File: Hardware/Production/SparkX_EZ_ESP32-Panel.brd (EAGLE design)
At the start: 187.2 x 95.5 mm, 1506 parts, among them Q1 MBT3904DW1T1, Q10 MBT3904DW1T1, Q11 MBT3904DW1T1, Q12 MBT3904DW1T1, Q13 MBT3904DW1T1, Q14 MBT3904DW1T1, Q15 MBT3904DW1T1, Q16 MBT3904DW1T1, Q17 MBT3904DW1T1, Q18 MBT3904DW1T1, Q19 MBT3904DW1T1, Q2 MBT3904DW1T1, Q20 MBT3904DW1T1, Q3 MBT3904DW1T1, Q4 MBT3904DW1T1, Q5 MBT3904DW1T1, Q6 MBT3904DW1T1, Q7 MBT3904DW1T1, Q8 MBT3904DW1T1, Q9 MBT3904DW1T1, U1 MIC5219 3.3V, U10 W25QXX128MBIT-6X5-SKINNY_CENT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, U11 CP2102N, U12 MIC5219 3.3V, U13 ESP32, U14 W25QXX128MBIT-6X5-SKINNY_CENT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, U15 CP2102N, U16 MIC5219 3.3V, U17 ESP32, U18 W25QXX128MBIT-6X5-SKINNY_CENT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, U19 CP2102N, U2 ESP32, U20 MIC5219 3.3V, U21 ESP32, U22 W25QXX128MBIT-6X5-SKINNY_CENT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, U23 CP2102N, U24 MIC5219 3.3V, U25 ESP32, U26 W25QXX128MBIT-6X5-SKINNY_CENT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, U27 CP2102N, U28 MIC5219 3.3V, U29 ESP32, U3 W25QXX128MBIT-6X5-SKINNY_CENT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, U30 W25QXX128MBIT-6X5-SKINNY_CENT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, U31 CP2102N, U32 MIC5219 3.3V, U33 ESP32, U34 W25QXX128MBIT-6X5-SKINNY_CENT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, U35 CP2102N, U36 MIC5219 3.3V, U37 ESP32, U38 W25QXX128MBIT-6X5-SKINNY_CENT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, U39 CP2102N, U4 CP2102N, U40 MIC5219 3.3V, U41 ESP32, U42 W25QXX128MBIT-6X5-SKINNY_CENT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, U43 CP2102N, U44 MIC5219 3.3V, U45 ESP32, U46 W25QXX128MBIT-6X5-SKINNY_CENT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, U47 CP2102N, U48 MIC5219 3.3V, U49 ESP32, U5 ESP32, U50 W25QXX128MBIT-6X5-SKINNY_CENT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, U51 CP2102N, U52 MIC5219 3.3V, U53 ESP32, U54 W25QXX128MBIT-6X5-SKINNY_CENT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, U55 CP2102N, U56 MIC5219 3.3V, U57 ESP32, U58 W25QXX128MBIT-6X5-SKINNY_CENT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, U59 CP2102N, U6 W25QXX128MBIT-6X5-SKINNY_CENT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, U60 MIC5219 3.3V, U61 ESP32, U62 W25QXX128MBIT-6X5-SKINNY_CENT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, U63 CP2102N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

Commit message: Post-review updates
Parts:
- C1, C122, C147, C172, C197, C222, C247, C272, C297, C322, C347, C372, C397, C422, C447, C47, C472, C497, C72, C97: value 0.1uF -> 2.2uF
- moved C204 1.17 mm to (139.6, 20.5)
- moved C229 1.17 mm to (155.9, 20.5)
- moved C179 1.17 mm to (123.4, 20.5)
- moved C329 1.17 mm to (49.8, 61.3)
- moved C354 1.17 mm to (66.1, 61.3)
- moved C379 1.17 mm to (82.4, 61.3)
- moved C404 1.17 mm to (98.6, 61.3)
- moved C429 1.17 mm to (114.9, 61.3)
- moved C279 1.17 mm to (17.3, 61.3)
- moved C29 1.17 mm to (25.8, 20.5)
- moved C254 1.17 mm to (1.08, 61.3)
- moved C11 1.17 mm to (9.59, 20.5)
- moved C304 1.17 mm to (33.6, 61.3)
- moved C54 1.17 mm to (42.1, 20.5)
- moved C79 1.17 mm to (58.4, 20.5)
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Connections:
- net CS1: now also U2.17; no longer U2.15
- net CS10: now also U13.17; no longer U13.15
- net CS11: now also U13.20; no longer U13.16
- net CS13: now also U17.17; no longer U17.15
- net CS14: now also U17.20; no longer U17.16
- net CS16: now also U21.17; no longer U21.15
- net CS17: now also U21.20; no longer U21.16
- net CS19: now also U25.17; no longer U25.15
- net CS2: now also U2.20; no longer U2.16
- net CS20: now also U25.20; no longer U25.16
- net CS22: now also U29.17; no longer U29.15
- net CS23: now also U29.20; no longer U29.16
- net CS25: now also U33.17; no longer U33.15
- net CS26: now also U33.20; no longer U33.16
- net CS28: now also U37.17; no longer U37.15
- net CS29: now also U37.20; no longer U37.16
- net CS31: now also U41.17; no longer U41.15
- net CS32: now also U41.20; no longer U41.16
- net CS34: now also U45.17; no longer U45.15
- net CS35: now also U45.20; no longer U45.16
- net CS37: now also U49.17; no longer U49.15
- net CS38: now also U49.20; no longer U49.16
- net CS4: now also U5.17; no longer U5.15
- net CS40: now also U53.17; no longer U53.15
- net CS41: now also U53.20; no longer U53.16
- net CS43: now also U57.17; no longer U57.15
- net CS44: now also U57.20; no longer U57.16
- net CS46: now also U61.17; no longer U61.15
- net CS47: now also U61.20; no longer U61.16
- net CS49: now also U65.17; no longer U65.15
- net CS5: now also U5.20; no longer U5.16
- net CS50: now also U65.20; no longer U65.16
- net CS52: now also U69.17; no longer U69.15
- net CS53: now also U69.20; no longer U69.16
- net CS55: now also U73.17; no longer U73.15
- net CS56: now also U73.20; no longer U73.16
- net CS58: now also U77.17; no longer U77.15
- net CS59: now also U77.20; no longer U77.16
- net CS7: now also U9.17; no longer U9.15
- net CS8: now also U9.20; no longer U9.16
- net GPIO0: now also U2.16; no longer U2.10
- net GPIO1: now also U2.15; no longer U2.11
- net GPIO10: now also U21.16; no longer U21.10
- net GPIO11: now also U21.15; no longer U21.11
- net GPIO12: now also U25.16; no longer U25.10
- net GPIO13: now also U25.15; no longer U25.11
- net GPIO14: now also U29.16; no longer U29.10
- net GPIO15: now also U29.15; no longer U29.11
- net GPIO16: now also U33.16; no longer U33.10
- net GPIO17: now also U33.15; no longer U33.11
- net GPIO18: now also U37.16; no longer U37.10
- net GPIO19: now also U37.15; no longer U37.11
- net GPIO2: now also U5.16; no longer U5.10
- net GPIO20: now also U41.16; no longer U41.10
- net GPIO21: now also U41.15; no longer U41.11
- net GPIO22: now also U45.16; no longer U45.10
- net GPIO23: now also U45.15; no longer U45.11
- net GPIO24: now also U49.16; no longer U49.10
- net GPIO25: now also U49.15; no longer U49.11
- net GPIO26: now also U53.16; no longer U53.10
- net GPIO27: now also U53.15; no longer U53.11
- net GPIO28: now also U57.16; no longer U57.10
- net GPIO29: now also U57.15; no longer U57.11
- net GPIO3: now also U5.15; no longer U5.11
- net GPIO30: now also U61.16; no longer U61.10
- net GPIO31: now also U61.15; no longer U61.11
- net GPIO32: now also U65.16; no longer U65.10
- net GPIO33: now also U65.15; no longer U65.11
- net GPIO34: now also U69.16; no longer U69.10
- net GPIO35: now also U69.15; no longer U69.11
- net GPIO36: now also U73.16; no longer U73.10
- net GPIO37: now also U73.15; no longer U73.11
- net GPIO38: now also U77.16; no longer U77.10
- net GPIO39: now also U77.15; no longer U77.11
- net GPIO4: now also U9.16; no longer U9.10
- net GPIO5: now also U9.15; no longer U9.11
- net GPIO6: now also U13.16; no longer U13.10
- net GPIO7: now also U13.15; no longer U13.11
- net GPIO8: now also U17.16; no longer U17.10
- net GPIO9: now also U17.15; no longer U17.11
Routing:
- net SDA9: track 69.7 -> 50.0 mm
- net SDA8: track 69.7 -> 50.0 mm
- net SDA4: track 69.7 -> 50.0 mm
- net SDA13: track 69.7 -> 50.0 mm
- net SDA12: track 69.7 -> 50.0 mm
- net SDA1: track 69.7 -> 50.0 mm
- net SDA: track 69.7 -> 50.0 mm
- net SDA11: track 69.7 -> 50.0 mm
- net SDA10: track 69.7 -> 50.0 mm
- net SDA3: track 69.7 -> 50.0 mm
- net SDA2: track 69.7 -> 50.0 mm
- net SDA17: track 69.7 -> 50.0 mm
- net SDA16: track 69.7 -> 50.0 mm
- net SDA15: track 69.7 -> 50.0 mm
- net SDA14: track 69.7 -> 50.0 mm
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
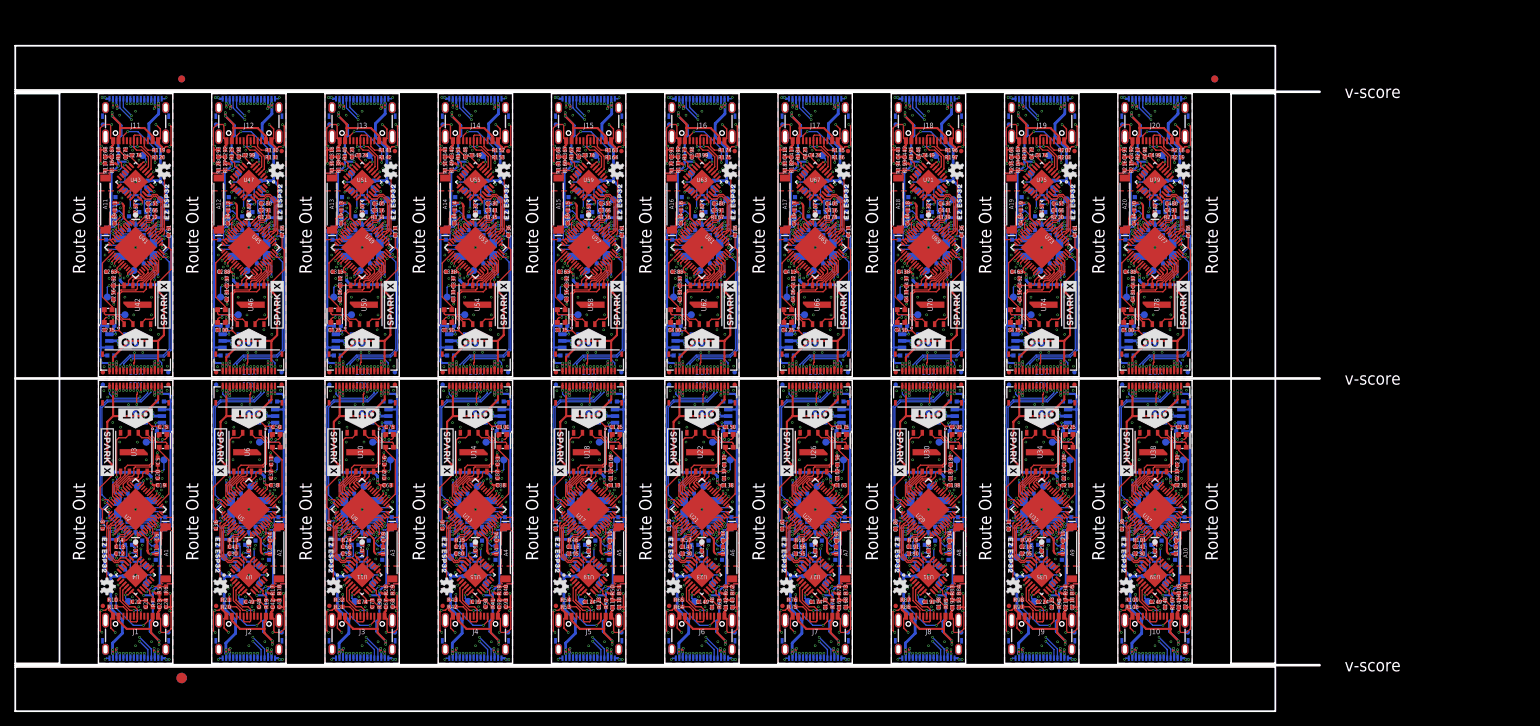
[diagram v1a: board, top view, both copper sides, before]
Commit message: Gapless production panel
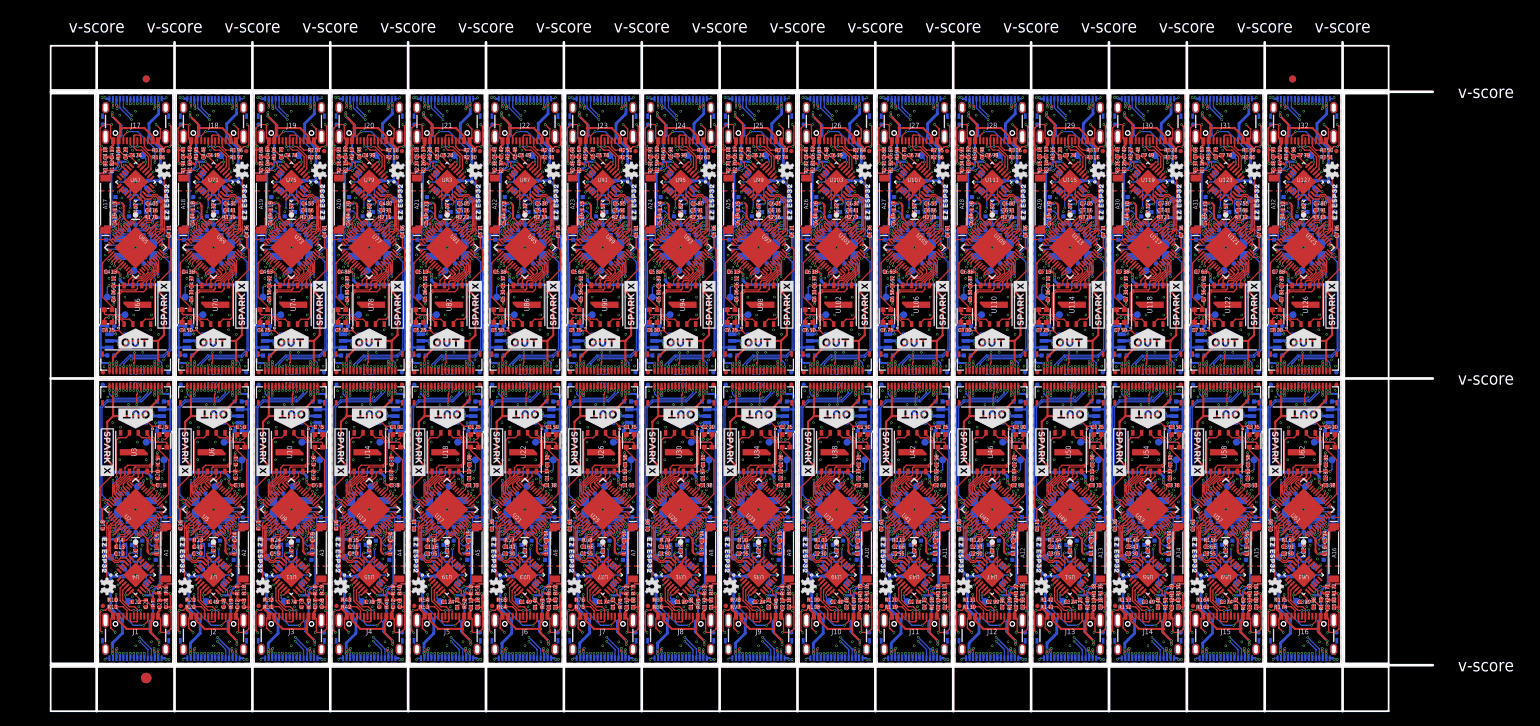
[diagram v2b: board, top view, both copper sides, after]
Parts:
- added !BOOT!20, !BOOT!21, !BOOT!22, !BOOT!23, !BOOT!24, !BOOT!25, !BOOT!26, !BOOT!27, !BOOT!28, !BOOT!29, !BOOT!30, !BOOT!31, !RESET!20, !RESET!21, !RESET!22, !RESET!23, !RESET!24, !RESET!25, !RESET!26, !RESET!27, !RESET!28, !RESET!29, !RESET!30, !RESET!31, FLASH_VDD20, FLASH_VDD21, FLASH_VDD22, FLASH_VDD23, FLASH_VDD24, FLASH_VDD25, FLASH_VDD26, FLASH_VDD27, FLASH_VDD28, FLASH_VDD29, FLASH_VDD30, FLASH_VDD31, LED_DO20, LED_DO21, LED_DO22, LED_DO23, LED_DO24, LED_DO25, LED_DO26, LED_DO27, LED_DO28, LED_DO29, LED_DO30, LED_DO31, RXT20, RXT21, RXT22, RXT23, RXT24, RXT25, RXT26, RXT27, RXT28, RXT29, RXT30, RXT31, TXT20, TXT21, TXT22, TXT23, TXT24, TXT25, TXT26, TXT27, TXT28, TXT29, TXT30, TXT31, USB_3V21, USB_3V22, USB_3V23, USB_3V24, USB_3V25, USB_3V26, USB_3V27, USB_3V28, USB_3V29, USB_3V30, USB_3V31, USB_3V32: TEST-POINT3X4, SparkFun-Connectors:PAD.03X.04
- added A21, A22, A23, A24, A25, A26, A27, A28, A29, A30, A31, A32: ANTENNA2.4GHZ-8.0X1.0MM, SparkFun-RF:ANT-2.4GHZ-8.0X1.0MM
- added C501, C502, C526, C527, C551, C552, C576, C577, C601, C602, C626, C627, C651, C652, C676, C677, C701, C702, C726, C727, C751, C752, C776, C777: 12pF, SparkFun-Capacitors:0402-TIGHT
- added C503, C504, C528, C529, C553, C554, C578, C579, C603, C604, C628, C629, C653, C654, C678, C679, C703, C704, C728, C729, C753, C754, C778, C779: 270pF, SparkFun-Capacitors:0402-TIGHT
- added C505, C530, C555, C580, C605, C630, C655, C680, C705, C730, C755, C780: 10nF, SparkFun-Capacitors:0402-TIGHT
- added C506, C508, C509, C511, C513, C517, C524, C525, C531, C533, C534, C536, C538, C542, C549, C550, C556, C558, C559, C561, C563, C567, C574, C575, C581, C583, C584, C586, C588, C592, C599, C600, C606, C608, C609, C611, C613, C617, C624, C625, C631, C633, C634, C636, C638, C642, C649, C650, C656, C658, C659, C661, C663, C667, C674, C675, C681, C683, C684, C686, C688, C692, C699, C700, C706, C708, C709, C711, C713, C717, C724, C725, C731, C733, C734, C736, C738, C742, C749, C750, C756, C758, C759, C761, C763, C767, C774, C775, C781, C783, C784, C786, C788, C792, C799, C800: 0.1uF, SparkFun-Capacitors:0402-TIGHT
- added C507, C532, C557, C582, C607, C632, C657, C682, C707, C732, C757, C782: 100pF, SparkFun-Capacitors:0402-TIGHT
- added C510, C535, C560, C585, C610, C635, C660, C685, C710, C735, C760, C785: 10uF, SparkFun-Capacitors:0402-TIGHT
- added C512, C537, C562, C587, C612, C637, C662, C687, C712, C737, C762, C787: 1.0uF, SparkFun-Capacitors:0402-TIGHT
- added C514, C515, C539, C540, C564, C565, C589, C590, C614, C615, C639, C640, C664, C665, C689, C690, C714, C715, C739, C740, C764, C765, C789, C790: 15pF, SparkFun-Capacitors:0402-TIGHT
- added C516, C541, C566, C591, C616, C641, C666, C691, C716, C741, C766, C791: 3.0nF, SparkFun-Capacitors:0402-TIGHT
- added C518, C523, C543, C548, C568, C573, C593, C598, C618, C623, C643, C648, C668, C673, C693, C698, C718, C723, C743, C748, C768, C773, C793, C798: 4.7uF, SparkFun-Capacitors:0402-TIGHT
- added C519, C520, C544, C545, C569, C570, C594, C595, C619, C620, C644, C645, C669, C670, C694, C695, C719, C720, C744, C745, C769, C770, C794, C795: DNP, SparkFun-Capacitors:0402-TIGHT
- added C521, C522, C546, C547, C571, C572, C596, C597, C621, C622, C646, C647, C671, C672, C696, C697, C721, C722, C746, C747, C771, C772, C796, C797: 2.2uF, SparkFun-Capacitors:0402-TIGHT
- added D21, D22, D23, D24, D25, D26, D27, D28, D29, D30, D31, D32: WS2812_2020, SparkFun-LED:WS2812-2020
- added FD100, FD101, FD102, FD103, FD104, FD105, FD106, FD107, FD108, FD109, FD110, FD111, FD112, FD113, FD114, FD115, FD116, FD117, FD118, FD119, FD120, FD121, FD122, FD123, FD124, FD125, FD126, FD127, FD128, FD81, FD82, FD83, FD84, FD85, FD86, FD87, FD88, FD89, FD90, FD91, FD92, FD93, FD94, FD95, FD96, FD97, FD98, FD99: FIDUCIALUFIDUCIAL, SparkFun-Aesthetics:FIDUCIAL-MICRO
- added IN20, IN21, IN22, IN23, IN24, IN25, IN26, IN27, IN28, IN29, IN30, IN31, OUT20, OUT21, OUT22, OUT23, OUT24, OUT25, OUT26, OUT27, OUT28, OUT29, OUT30, OUT31: FPC_16_0.5MM_BACKFLIP, New_Parts_Connectors:FPC_16_DOUBLESIDED_BACKFLIP
- added J21, J22, J23, J24, J25, J26, J27, J28, J29, J30, J31, J32: (no value), SparkFun-Connectors:USB-C-16P_4LAYER-PADS
- added L21, L22, L23, L24, L25, L26, L27, L28, L29, L30, L31, L32: 0, SparkFun-Resistors:0402-TIGHT
- added LOGO41, LOGO42, LOGO43, LOGO44, LOGO45, LOGO46, LOGO47, LOGO48, LOGO49, LOGO50, LOGO51, LOGO52, LOGO53, LOGO54, LOGO55, LOGO56, LOGO57, LOGO58, LOGO59, LOGO60, LOGO61, LOGO62, LOGO63, LOGO64: OSHW-LOGOMINI, SparkFun-Aesthetics:OSHW-LOGO-MINI
- added Q21, Q22, Q23, Q24, Q25, Q26, Q27, Q28, Q29, Q30, Q31, Q32: MBT3904DW1T1, SparkFun-DiscreteSemi:SC70-6
- added R221, R223, R224, R225, R232, R234, R235, R236, R243, R245, R246, R247, R254, R256, R257, R258, R265, R267, R268, R269, R276, R278, R279, R280, R287, R289, R290, R291, R298, R300, R301, R302, R309, R311, R312, R313, R320, R322, R323, R324, R331, R333, R334, R335, R342, R344, R345, R346: 10k, SparkFun-Resistors:0402-TIGHT
- added R222, R233, R244, R255, R266, R277, R288, R299, R310, R321, R332, R343: 20k, SparkFun-Resistors:0402-TIGHT
- added R226, R237, R248, R259, R270, R281, R292, R303, R314, R325, R336, R347: 22k, SparkFun-Resistors:0402-TIGHT
- added R227, R238, R249, R260, R271, R282, R293, R304, R315, R326, R337, R348: 33k, SparkFun-Resistors:0402-TIGHT
- added R228, R239, R250, R261, R272, R283, R294, R305, R316, R327, R338, R349: 2.2k, SparkFun-Resistors:0402-TIGHT
- added R229, R230, R240, R241, R251, R252, R262, R263, R273, R274, R284, R285, R295, R296, R306, R307, R317, R318, R328, R329, R339, R340, R350, R351: 5.1k, SparkFun-Resistors:0402-TIGHT
- added R231, R242, R253, R264, R275, R286, R297, R308, R319, R330, R341, R352: 100k, SparkFun-Resistors:0402-TIGHT
- added U$261, U$262, U$274, U$275, U$287, U$288, U$300, U$301, U$313, U$314, U$326, U$327, U$339, U$340, U$352, U$353, U$365, U$366, U$378, U$379, U$391, U$392, U$404, U$405: SPARKX-LOGO3, SparkX:SPARKX-SMALL
- added U$263, U$276, U$289, U$302, U$315, U$328, U$341, U$354, U$367, U$380, U$393, U$406: (no value), output:#IN#0
- added U$264, U$277, U$290, U$303, U$316, U$329, U$342, U$355, U$368, U$381, U$394, U$407: (no value), output:#OUT#0
- added U$265, U$266, U$278, U$279, U$291, U$292, U$304, U$305, U$317, U$318, U$330, U$331, U$343, U$344, U$356, U$357, U$369, U$370, U$382, U$383, U$395, U$396, U$408, U$409: (no value), output:EZ_ESP320
- added U$267, U$280, U$293, U$306, U$319, U$332, U$345, U$358, U$371, U$384, U$397, U$410: (no value), output:#TXT#0
- added U$268, U$281, U$294, U$307, U$320, U$333, U$346, U$359, U$372, U$385, U$398, U$411: (no value), output:#RXT#0
- added U$269, U$282, U$295, U$308, U$321, U$334, U$347, U$360, U$373, U$386, U$399, U$412: (no value), output:##BOOT##0
- added U$270, U$283, U$296, U$309, U$322, U$335, U$348, U$361, U$374, U$387, U$400, U$413: (no value), output:##RESET##0
- added U$271, U$284, U$297, U$310, U$323, U$336, U$349, U$362, U$375, U$388, U$401, U$414: (no value), output:#USB_3V3#0
- added U$272, U$285, U$298, U$311, U$324, U$337, U$350, U$363, U$376, U$389, U$402, U$415: (no value), output:#FVDD#0
- added U$273, U$286, U$299, U$312, U$325, U$338, U$351, U$364, U$377, U$390, U$403, U$416: (no value), output:#LED_DO#0
- added U100, U104, U108, U112, U116, U120, U124, U128, U84, U88, U92, U96: MIC5219 3.3V, SparkFun-IC-Power:SOT23-5
- added U101, U105, U109, U113, U117, U121, U125, U81, U85, U89, U93, U97: ESP32, SparkFun-RF:QFN48-0.4MM
- added U102, U106, U110, U114, U118, U122, U126, U82, U86, U90, U94, U98: W25QXX128MBIT-6X5-SKINNY_CENTER, SparkFun-IC-Memory:WSON-8-6X5-SKINNY_CENTERPAD
- added U103, U107, U111, U115, U119, U123, U127, U83, U87, U91, U95, U99: CP2102N, SparkFun-IC-Comms:QFN24
- added X41, X43, X45, X47, X49, X51, X53, X55, X57, X59, X61, X63: 40MHz, SparkFun-Clocks:CRYSTAL-SMD-2X2.5MM
- added X42, X44, X46, X48, X50, X52, X54, X56, X58, X60, X62, X64: 32.768kHz, SparkFun-Clocks:CRYSTAL-SMD-3.2X1.5MM
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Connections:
- new net !RESET20: !RESET!20.1, Q21.3, R221.1, U81.9
- new net !RESET21: !RESET!21.1, Q22.3, R232.1, U85.9
- new net !RESET22: !RESET!22.1, Q23.3, R243.1, U89.9
- new net !RESET23: !RESET!23.1, Q24.3, R254.1, U93.9
- new net !RESET24: !RESET!24.1, Q25.3, R265.1, U97.9
- new net !RESET25: !RESET!25.1, Q26.3, R276.1, U101.9
- new net !RESET26: !RESET!26.1, Q27.3, R287.1, U105.9
- new net !RESET27: !RESET!27.1, Q28.3, R298.1, U109.9
- new net !RESET28: !RESET!28.1, Q29.3, R309.1, U113.9
- new net !RESET29: !RESET!29.1, Q30.3, R320.1, U117.9
- new net !RESET30: !RESET!30.1, Q31.3, R331.1, U121.9
- new net !RESET31: !RESET!31.1, Q32.3, R342.1, U125.9
- new net 0-!BOOT!20: !BOOT!20.1, Q21.6, R225.1, U81.23
- new net 0-!BOOT!21: !BOOT!21.1, Q22.6, R236.1, U85.23
- new net 0-!BOOT!22: !BOOT!22.1, Q23.6, R247.1, U89.23
- new net 0-!BOOT!23: !BOOT!23.1, Q24.6, R258.1, U93.23
- new net 0-!BOOT!24: !BOOT!24.1, Q25.6, R269.1, U97.23
- new net 0-!BOOT!25: !BOOT!25.1, Q26.6, R280.1, U101.23
- new net 0-!BOOT!26: !BOOT!26.1, Q27.6, R291.1, U105.23
- new net 0-!BOOT!27: !BOOT!27.1, Q28.6, R302.1, U109.23
- new net 0-!BOOT!28: !BOOT!28.1, Q29.6, R313.1, U113.23
- new net 0-!BOOT!29: !BOOT!29.1, Q30.6, R324.1, U117.23
- new net 0-!BOOT!30: !BOOT!30.1, Q31.6, R335.1, U121.23
- new net 0-!BOOT!31: !BOOT!31.1, Q32.6, R346.1, U125.23
- new net 3.3V20: C507.1, C508.1, C509.1, C510.1, C511.1, C513.1, C521.1, C525.1, D21.VCC, IN20.15, IN20.2, OUT20.15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
- new net 3.3V21: C532.1, C533.1, C534.1, C535.1, C536.1, C538.1, C546.1, C550.1, D22.VCC, IN21.15, IN21.2, OUT21.15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
- new net 3.3V22: C557.1, C558.1, C559.1, C560.1, C561.1, C563.1, C571.1, C575.1, D23.VCC, IN22.15, IN22.2, OUT22.15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
- new net 3.3V23: C582.1, C583.1, C584.1, C585.1, C586.1, C588.1, C596.1, C600.1, D24.VCC, IN23.15, IN23.2, OUT23.15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
- new net 3.3V24: C607.1, C608.1, C609.1, C610.1, C611.1, C613.1, C621.1, C625.1, D25.VCC, IN24.15, IN24.2, OUT24.15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
- new net 3.3V25: C632.1, C633.1, C634.1, C635.1, C636.1, C638.1, C646.1, C650.1, D26.VCC, IN25.15, IN25.2, OUT25.15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
- new net 3.3V26: C657.1, C658.1, C659.1, C660.1, C661.1, C663.1, C671.1, C675.1, D27.VCC, IN26.15, IN26.2, OUT26.15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
- new net 3.3V27: C682.1, C683.1, C684.1, C685.1, C686.1, C688.1, C696.1, C700.1, D28.VCC, IN27.15, IN27.2, OUT27.15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
- new net 3.3V28: C707.1, C708.1, C709.1, C710.1, C711.1, C713.1, C721.1, C725.1, D29.VCC, IN28.15, IN28.2, OUT28.15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
- new net 3.3V29: C732.1, C733.1, C734.1, C735.1, C736.1, C738.1, C746.1, C750.1, D30.VCC, IN29.15, IN29.2, OUT29.15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
- new net 3.3V30: C757.1, C758.1, C759.1, C760.1, C761.1, C763.1, C771.1, C775.1, D31.VCC, IN30.15, IN30.2, OUT30.15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
- new net 3.3V31: C782.1, C783.1, C784.1, C785.1, C786.1, C788.1, C796.1, C800.1, D32.VCC, IN31.15, IN31.2, OUT31.15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
- new net 32-RTC20: C514.2, U81.12, X42.P$1
- new net 32-RTC21: C539.2, U85.12, X44.P$1
- new net 32-RTC22: C564.2, U89.12, X46.P$1
- new net 32-RTC23: C589.2, U93.12, X48.P$1
- new net 32-RTC24: C614.2, U97.12, X50.P$1
- new net 32-RTC25: C639.2, U101.12, X52.P$1
- new net 32-RTC26: C664.2, U105.12, X54.P$1
- new net 32-RTC27: C689.2, U109.12, X56.P$1
- new net 32-RTC28: C714.2, U113.12, X58.P$1
- new net 32-RTC29: C739.2, U117.12, X60.P$1
- new net 32-RTC30: C764.2, U121.12, X62.P$1
- new net 32-RTC31: C789.2, U125.12, X64.P$1
- new net 33-RTC20: C515.2, U81.13, X42.P$2
- new net 33-RTC21: C540.2, U85.13, X44.P$2
- new net 33-RTC22: C565.2, U89.13, X46.P$2
- new net 33-RTC23: C590.2, U93.13, X48.P$2
- new net 33-RTC24: C615.2, U97.13, X50.P$2
- new net 33-RTC25: C640.2, U101.13, X52.P$2
- new net 33-RTC26: C665.2, U105.13, X54.P$2
- new net 33-RTC27: C690.2, U109.13, X56.P$2
- new net 33-RTC28: C715.2, U113.13, X58.P$2
- new net 33-RTC29: C740.2, U117.13, X60.P$2
- new net 33-RTC30: C765.2, U121.13, X62.P$2
- new net 33-RTC31: C790.2, U125.13, X64.P$2
- new net 61: C504.1, U81.7
- new net 62: C503.2, U81.5
- new net 63: C503.1, U81.6
- new net 64: C529.1, U85.7
- new net 65: C528.2, U85.5
- new net 66: C528.1, U85.6
- new net 67: C554.1, U89.7
- new net 68: C553.2, U89.5
- new net 69: C553.1, U89.6
- new net 70: C579.1, U93.7
- new net 71: C578.2, U93.5
- new net 72: C578.1, U93.6
- new net 73: C604.1, U97.7
- new net 74: C603.2, U97.5
- new net 75: C603.1, U97.6
- new net 76: C629.1, U101.7
- new net 77: C628.2, U101.5
- new net 78: C628.1, U101.6
- new net 79: C654.1, U105.7
- new net 80: C653.2, U105.5
- new net 81: C653.1, U105.6
- new net 82: C679.1, U109.7
- new net 83: C678.2, U109.5
- new net 84: C678.1, U109.6
- new net 85: C704.1, U113.7
- new net 86: C703.2, U113.5
- new net 87: C703.1, U113.6
- new net 88: C729.1, U117.7
- new net 89: C728.2, U117.5
- new net 90: C728.1, U117.6
- new net 91: C754.1, U121.7
- new net 92: C753.2, U121.5
- new net 93: C753.1, U121.6
- new net 94: C779.1, U125.7
- new net 95: C778.2, U125.5
- new net 96: C778.1, U125.6
- new net CAP_10N21: C505.2, C516.1, R222.2, U81.48
- new net CAP_10N22: C530.2, C541.1, R233.2, U85.48
- new net CAP_10N23: C555.2, C566.1, R244.2, U89.48
- new net CAP_10N24: C580.2, C591.1, R255.2, U93.48
- new net CAP_10N25: C605.2, C616.1, R266.2, U97.48
- new net CAP_10N26: C630.2, C641.1, R277.2, U101.48
- new net CAP_10N27: C655.2, C666.1, R288.2, U105.48
- new net CAP_10N28: C680.2, C691.1, R299.2, U109.48
- new net CAP_10N29: C705.2, C716.1, R310.2, U113.48
- new net CAP_10N30: C730.2, C741.1, R321.2, U117.48
- new net CAP_10N31: C755.2, C766.1, R332.2, U121.48
- new net CAP_10N32: C780.2, C791.1, R343.2, U125.48
- new net CIPO20: IN20.6, OUT20.6, U81.38
- new net CIPO21: IN21.6, OUT21.6, U85.38
- new net CIPO22: IN22.6, OUT22.6, U89.38
- new net CIPO23: IN23.6, OUT23.6, U93.38
- new net CIPO24: IN24.6, OUT24.6, U97.38
- new net CIPO25: IN25.6, OUT25.6, U101.38
- new net CIPO26: IN26.6, OUT26.6, U105.38
- new net CIPO27: IN27.6, OUT27.6, U109.38
- new net CIPO28: IN28.6, OUT28.6, U113.38
- new net CIPO29: IN29.6, OUT29.6, U117.38
- new net CIPO30: IN30.6, OUT30.6, U121.38
- new net CIPO31: IN31.6, OUT31.6, U125.38
- new net COPI20: IN20.5, OUT20.5, U81.36
- new net COPI21: IN21.5, OUT21.5, U85.36
- new net COPI22: IN22.5, OUT22.5, U89.36
- new net COPI23: IN23.5, OUT23.5, U93.36
- new net COPI24: IN24.5, OUT24.5, U97.36
- new net COPI25: IN25.5, OUT25.5, U101.36
- new net COPI26: IN26.5, OUT26.5, U105.36
- new net COPI27: IN27.5, OUT27.5, U109.36
- new net COPI28: IN28.5, OUT28.5, U113.36
- new net COPI29: IN29.5, OUT29.5, U117.36
- new net COPI30: IN30.5, OUT30.5, U121.36
- new net COPI31: IN31.5, OUT31.5, U125.36
- new net CS60: IN20.7, OUT20.7, U81.34
- new net CS61: IN20.8, OUT20.8, U81.17
- new net CS62: IN20.9, OUT20.9, U81.20
- new net CS63: IN21.7, OUT21.7, U85.34
- new net CS64: IN21.8, OUT21.8, U85.17
- new net CS65: IN21.9, OUT21.9, U85.20
- new net CS66: IN22.7, OUT22.7, U89.34
- new net CS67: IN22.8, OUT22.8, U89.17
- new net CS68: IN22.9, OUT22.9, U89.20
- new net CS69: IN23.7, OUT23.7, U93.34
- new net CS70: IN23.8, OUT23.8, U93.17
- new net CS71: IN23.9, OUT23.9, U93.20
- new net CS72: IN24.7, OUT24.7, U97.34
- new net CS73: IN24.8, OUT24.8, U97.17
- new net CS74: IN24.9, OUT24.9, U97.20
- new net CS75: IN25.7, OUT25.7, U101.34
- new net CS76: IN25.8, OUT25.8, U101.17
- new net CS77: IN25.9, OUT25.9, U101.20
- new net CS78: IN26.7, OUT26.7, U105.34
- new net CS79: IN26.8, OUT26.8, U105.17
- new net CS80: IN26.9, OUT26.9, U105.20
- new net CS81: IN27.7, OUT27.7, U109.34
- new net CS82: IN27.8, OUT27.8, U109.17
- new net CS83: IN27.9, OUT27.9, U109.20
- new net CS84: IN28.7, OUT28.7, U113.34
- new net CS85: IN28.8, OUT28.8, U113.17
- new net CS86: IN28.9, OUT28.9, U113.20
- new net CS87: IN29.7, OUT29.7, U117.34
- new net CS88: IN29.8, OUT29.8, U117.17
- new net CS89: IN29.9, OUT29.9, U117.20
- new net CS90: IN30.7, OUT30.7, U121.34
- new net CS91: IN30.8, OUT30.8, U121.17
- new net CS92: IN30.9, OUT30.9, U121.20
- new net CS93: IN31.7, OUT31.7, U125.34
- new net CS94: IN31.8, OUT31.8, U125.17
- new net CS95: IN31.9, OUT31.9, U125.20
- new net D+20: J21.A6, J21.B6, U83.3
- new net D+21: J22.A6, J22.B6, U87.3
- new net D+22: J23.A6, J23.B6, U91.3
- new net D+23: J24.A6, J24.B6, U95.3
- new net D+24: J25.A6, J25.B6, U99.3
- new net D+25: J26.A6, J26.B6, U103.3
- new net D+26: J27.A6, J27.B6, U107.3
- new net D+27: J28.A6, J28.B6, U111.3
- new net D+28: J29.A6, J29.B6, U115.3
- new net D+29: J30.A6, J30.B6, U119.3
- new net D+30: J31.A6, J31.B6, U123.3
- new net D+31: J32.A6, J32.B6, U127.3
- new net D-20: J21.A7, J21.B7, U83.4
- new net D-21: J22.A7, J22.B7, U87.4
- new net D-22: J23.A7, J23.B7, U91.4
- new net D-23: J24.A7, J24.B7, U95.4
- new net D-24: J25.A7, J25.B7, U99.4
- new net D-25: J26.A7, J26.B7, U103.4
- new net D-26: J27.A7, J27.B7, U107.4
- new net D-27: J28.A7, J28.B7, U111.4
- new net D-28: J29.A7, J29.B7, U115.4
- new net D-29: J30.A7, J30.B7, U119.4
- new net D-30: J31.A7, J31.B7, U123.4
- new net D-31: J32.A7, J32.B7, U127.4
- new net DTR20: Q21.1, R223.1, U83.23
- new net DTR21: Q22.1, R234.1, U87.23
- new net DTR22: Q23.1, R245.1, U91.23
- new net DTR23: Q24.1, R256.1, U95.23
- new net DTR24: Q25.1, R267.1, U99.23
- new net DTR25: Q26.1, R278.1, U103.23
- new net DTR26: Q27.1, R289.1, U107.23
- new net DTR27: Q28.1, R300.1, U111.23
- new net DTR28: Q29.1, R311.1, U115.23
- new net DTR29: Q30.1, R322.1, U119.23
- new net DTR30: Q31.1, R333.1, U123.23
- new net DTR31: Q32.1, R344.1, U127.23
- new net FLASH_SCK20: U81.31, U82.6
- new net FLASH_SCK21: U85.31, U86.6
- new net FLASH_SCK22: U89.31, U90.6
- new net FLASH_SCK23: U93.31, U94.6
- new net FLASH_SCK24: U97.31, U98.6
- new net FLASH_SCK25: U101.31, U102.6
- new net FLASH_SCK26: U105.31, U106.6
- new net FLASH_SCK27: U109.31, U110.6
- new net FLASH_SCK28: U113.31, U114.6
- new net FLASH_SCK29: U117.31, U118.6
- new net FLASH_SCK30: U121.31, U122.6
- new net FLASH_SCK31: U125.31, U126.6
- new net FLASH_SCS20: U81.30, U82.1
- new net FLASH_SCS21: U85.30, U86.1
- new net FLASH_SCS22: U89.30, U90.1
- new net FLASH_SCS23: U93.30, U94.1
- new net FLASH_SCS24: U97.30, U98.1
- new net FLASH_SCS25: U101.30, U102.1
- new net FLASH_SCS26: U105.30, U106.1
- new net FLASH_SCS27: U109.30, U110.1
- new net FLASH_SCS28: U113.30, U114.1
- new net FLASH_SCS29: U117.30, U118.1
- new net FLASH_SCS30: U121.30, U122.1
- new net FLASH_SCS31: U125.30, U126.1
- new net FLASH_SDI20: U81.33, U82.5
- new net FLASH_SDI21: U85.33, U86.5
- new net FLASH_SDI22: U89.33, U90.5
- new net FLASH_SDI23: U93.33, U94.5
- new net FLASH_SDI24: U97.33, U98.5
- new net FLASH_SDI25: U101.33, U102.5
- new net FLASH_SDI26: U105.33, U106.5
- new net FLASH_SDI27: U109.33, U110.5
- new net FLASH_SDI28: U113.33, U114.5
- new net FLASH_SDI29: U117.33, U118.5
- new net FLASH_SDI30: U121.33, U122.5
- new net FLASH_SDI31: U125.33, U126.5
- new net FLASH_SDO20: U81.32, U82.2
- new net FLASH_SDO21: U85.32, U86.2
- new net FLASH_SDO22: U89.32, U90.2
- new net FLASH_SDO23: U93.32, U94.2
- new net FLASH_SDO24: U97.32, U98.2
- new net FLASH_SDO25: U101.32, U102.2
- new net FLASH_SDO26: U105.32, U106.2
- new net FLASH_SDO27: U109.32, U110.2
- new net FLASH_SDO28: U113.32, U114.2
- new net FLASH_SDO29: U117.32, U118.2
- new net FLASH_SDO30: U121.32, U122.2
- new net FLASH_SDO31: U125.32, U126.2
- new net FLASH_SHD20: U81.28, U82.7
- new net FLASH_SHD21: U85.28, U86.7
- new net FLASH_SHD22: U89.28, U90.7
- new net FLASH_SHD23: U93.28, U94.7
- new net FLASH_SHD24: U97.28, U98.7
- new net FLASH_SHD25: U101.28, U102.7
- new net FLASH_SHD26: U105.28, U106.7
- new net FLASH_SHD27: U109.28, U110.7
- new net FLASH_SHD28: U113.28, U114.7
- new net FLASH_SHD29: U117.28, U118.7
- new net FLASH_SHD30: U121.28, U122.7
- new net FLASH_SHD31: U125.28, U126.7
- new net FLASH_SWP20: U81.29, U82.3
- new net FLASH_SWP21: U85.29, U86.3
- new net FLASH_SWP22: U89.29, U90.3
- new net FLASH_SWP23: U93.29, U94.3
- new net FLASH_SWP24: U97.29, U98.3
- new net FLASH_SWP25: U101.29, U102.3
- new net FLASH_SWP26: U105.29, U106.3
- new net FLASH_SWP27: U109.29, U110.3
- new net FLASH_SWP28: U113.29, U114.3
- new net FLASH_SWP29: U117.29, U118.3
- new net FLASH_SWP30: U121.29, U122.3
- new net FLASH_SWP31: U125.29, U126.3
- new net FLASH_VDD20: C506.1, C512.1, FLASH_VDD20.1, U81.26, U82.8
- new net FLASH_VDD21: C531.1, C537.1, FLASH_VDD21.1, U85.26, U86.8
- new net FLASH_VDD22: C556.1, C562.1, FLASH_VDD22.1, U89.26, U90.8
- new net FLASH_VDD23: C581.1, C587.1, FLASH_VDD23.1, U93.26, U94.8
- new net FLASH_VDD24: C606.1, C612.1, FLASH_VDD24.1, U97.26, U98.8
- new net FLASH_VDD25: C631.1, C637.1, FLASH_VDD25.1, U101.26, U102.8
- new net FLASH_VDD26: C656.1, C662.1, FLASH_VDD26.1, U105.26, U106.8
- new net FLASH_VDD27: C681.1, C687.1, FLASH_VDD27.1, U109.26, U110.8
- new net FLASH_VDD28: C706.1, C712.1, FLASH_VDD28.1, U113.26, U114.8
- new net FLASH_VDD29: C731.1, C737.1, FLASH_VDD29.1, U117.26, U118.8
- new net FLASH_VDD30: C756.1, C762.1, FLASH_VDD30.1, U121.26, U122.8
- new net FLASH_VDD31: C781.1, C787.1, FLASH_VDD31.1, U125.26, U126.8
- new net GND20: C501.1, C502.1, C505.1, C506.2, C507.2, C508.2, C509.2, C510.2, C511.2, C512.2, C513.2, C514.1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
- new net GND21: C526.1, C527.1, C530.1, C531.2, C532.2, C533.2, C534.2, C535.2, C536.2, C537.2, C538.2, C539.1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
- new net GND22: C551.1, C552.1, C555.1, C556.2, C557.2, C558.2, C559.2, C560.2, C561.2, C562.2, C563.2, C564.1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
- new net GND23: C576.1, C577.1, C580.1, C581.2, C582.2, C583.2, C584.2, C585.2, C586.2, C587.2, C588.2, C589.1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
- new net GND24: C601.1, C602.1, C605.1, C606.2, C607.2, C608.2, C609.2, C610.2, C611.2, C612.2, C613.2, C614.1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
- new net GND25: C626.1, C627.1, C630.1, C631.2, C632.2, C633.2, C634.2, C635.2, C636.2, C637.2, C638.2, C639.1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
- new net GND26: C651.1, C652.1, C655.1, C656.2, C657.2, C658.2, C659.2, C660.2, C661.2, C662.2, C663.2, C664.1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
- new net GND27: C676.1, C677.1, C680.1, C681.2, C682.2, C683.2, C684.2, C685.2, C686.2, C687.2, C688.2, C689.1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
- new net GND28: C701.1, C702.1, C705.1, C706.2, C707.2, C708.2, C709.2, C710.2, C711.2, C712.2, C713.2, C714.1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
- new net GND29: C726.1, C727.1, C730.1, C731.2, C732.2, C733.2, C734.2, C735.2, C736.2, C737.2, C738.2, C739.1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
- new net GND30: C751.1, C752.1, C755.1, C756.2, C757.2, C758.2, C759.2, C760.2, C761.2, C762.2, C763.2, C764.1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
- new net GND31: C776.1, C777.1, C780.1, C781.2, C782.2, C783.2, C784.2, C785.2, C786.2, C787.2, C788.2, C789.1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
- new net GPIO40: IN20.10, OUT20.10, U81.16
- new net GPIO41: IN20.11, OUT20.11, U81.15
- new net GPIO42: IN21.10, OUT21.10, U85.16
- new net GPIO43: IN21.11, OUT21.11, U85.15
- new net GPIO44: IN22.10, OUT22.10, U89.16
- new net GPIO45: IN22.11, OUT22.11, U89.15
- new net GPIO46: IN23.10, OUT23.10, U93.16
- new net GPIO47: IN23.11, OUT23.11, U93.15
- new net GPIO48: IN24.10, OUT24.10, U97.16
- new net GPIO49: IN24.11, OUT24.11, U97.15
- new net GPIO50: IN25.10, OUT25.10, U101.16
- new net GPIO51: IN25.11, OUT25.11, U101.15
- new net GPIO52: IN26.10, OUT26.10, U105.16
- new net GPIO53: IN26.11, OUT26.11, U105.15
- new net GPIO54: IN27.10, OUT27.10, U109.16
- new net GPIO55: IN27.11, OUT27.11, U109.15
- new net GPIO56: IN28.10, OUT28.10, U113.16
- new net GPIO57: IN28.11, OUT28.11, U113.15
- new net GPIO58: IN29.10, OUT29.10, U117.16
- new net GPIO59: IN29.11, OUT29.11, U117.15
- new net GPIO60: IN30.10, OUT30.10, U121.16
- new net GPIO61: IN30.11, OUT30.11, U121.15
- new net GPIO62: IN31.10, OUT31.10, U125.16
- new net GPIO63: IN31.11, OUT31.11, U125.15
- new net LED20: D21.DI, U81.14
- new net LED21: D22.DI, U85.14
- new net LED22: D23.DI, U89.14
- new net LED23: D24.DI, U93.14
- new net LED24: D25.DI, U97.14
- new net LED25: D26.DI, U101.14
- new net LED26: D27.DI, U105.14
- new net LED27: D28.DI, U109.14
- new net LED28: D29.DI, U113.14
- new net LED29: D30.DI, U117.14
- new net LED30: D31.DI, U121.14
- new net LED31: D32.DI, U125.14
- new net N$261: Q21.5, R223.2
- new net N$262: Q21.2, R224.2
- new net N$263: C501.2, U81.45, X41.P1
- new net N$264: C502.2, U81.44, X41.P3
- new net N$265: C516.2, R222.1, U81.47
- new net N$266: R226.1, R227.2, U83.8
- new net N$267: R228.1, U83.9
- new net N$268: A21.FEED, C519.1, L21.1
- new net N$269: C520.1, L21.2, U81.2
- new net N$270: J21.A5, R229.2
- new net N$271: J21.B5, R230.2
- new net N$272: C504.2, U81.8
- new net N$273: D21.DO, LED_DO20.1
- new net N$274: Q22.5, R234.2
- new net N$275: Q22.2, R235.2
- new net N$276: C526.2, U85.45, X43.P1
- new net N$277: C527.2, U85.44, X43.P3
- new net N$278: C541.2, R233.1, U85.47
- new net N$279: R237.1, R238.2, U87.8
- new net N$280: R239.1, U87.9
- new net N$281: A22.FEED, C544.1, L22.1
- new net N$282: C545.1, L22.2, U85.2
- new net N$283: J22.A5, R240.2
- new net N$284: J22.B5, R241.2
- new net N$285: C529.2, U85.8
- new net N$286: D22.DO, LED_DO21.1
- new net N$287: Q23.5, R245.2
- new net N$288: Q23.2, R246.2
- new net N$289: C551.2, U89.45, X45.P1
- new net N$290: C552.2, U89.44, X45.P3
- new net N$291: C566.2, R244.1, U89.47
- new net N$292: R248.1, R249.2, U91.8
- new net N$293: R250.1, U91.9
- new net N$294: A23.FEED, C569.1, L23.1
- new net N$295: C570.1, L23.2, U89.2
- new net N$296: J23.A5, R251.2
- new net N$297: J23.B5, R252.2
- new net N$298: C554.2, U89.8
- new net N$299: D23.DO, LED_DO22.1
- new net N$300: Q24.5, R256.2
- new net N$301: Q24.2, R257.2
- new net N$302: C576.2, U93.45, X47.P1
- new net N$303: C577.2, U93.44, X47.P3
- new net N$304: C591.2, R255.1, U93.47
- new net N$305: R259.1, R260.2, U95.8
- new net N$306: R261.1, U95.9
- new net N$307: A24.FEED, C594.1, L24.1
- new net N$308: C595.1, L24.2, U93.2
- new net N$309: J24.A5, R262.2
- new net N$310: J24.B5, R263.2
- new net N$311: C579.2, U93.8
- new net N$312: D24.DO, LED_DO23.1
- new net N$313: Q25.5, R267.2
- new net N$314: Q25.2, R268.2
- new net N$315: C601.2, U97.45, X49.P1
- new net N$316: C602.2, U97.44, X49.P3
- new net N$317: C616.2, R266.1, U97.47
- new net N$318: R270.1, R271.2, U99.8
- new net N$319: R272.1, U99.9
- new net N$320: A25.FEED, C619.1, L25.1
- new net N$321: C620.1, L25.2, U97.2
- new net N$322: J25.A5, R273.2
- new net N$323: J25.B5, R274.2
- new net N$324: C604.2, U97.8
- new net N$325: D25.DO, LED_DO24.1
- new net N$326: Q26.5, R278.2
- new net N$327: Q26.2, R279.2
- new net N$328: C626.2, U101.45, X51.P1
- new net N$329: C627.2, U101.44, X51.P3
- new net N$330: C641.2, R277.1, U101.47
- new net N$331: R281.1, R282.2, U103.8
- new net N$332: R283.1, U103.9
- new net N$333: A26.FEED, C644.1, L26.1
- new net N$334: C645.1, L26.2, U101.2
- new net N$335: J26.A5, R284.2
- new net N$336: J26.B5, R285.2
- new net N$337: C629.2, U101.8
- new net N$338: D26.DO, LED_DO25.1
- new net N$339: Q27.5, R289.2
- new net N$340: Q27.2, R290.2
- new net N$341: C651.2, U105.45, X53.P1
- new net N$342: C652.2, U105.44, X53.P3
- new net N$343: C666.2, R288.1, U105.47
- new net N$344: R292.1, R293.2, U107.8
- new net N$345: R294.1, U107.9
- new net N$346: A27.FEED, C669.1, L27.1
- new net N$347: C670.1, L27.2, U105.2
- new net N$348: J27.A5, R295.2
- new net N$349: J27.B5, R296.2
- new net N$350: C654.2, U105.8
- new net N$351: D27.DO, LED_DO26.1
- new net N$352: Q28.5, R300.2
- new net N$353: Q28.2, R301.2
- new net N$354: C676.2, U109.45, X55.P1
- new net N$355: C677.2, U109.44, X55.P3
- new net N$356: C691.2, R299.1, U109.47
- new net N$357: R303.1, R304.2, U111.8
- new net N$358: R305.1, U111.9
- new net N$359: A28.FEED, C694.1, L28.1
- new net N$360: C695.1, L28.2, U109.2
- new net N$361: J28.A5, R306.2
- new net N$362: J28.B5, R307.2
- new net N$363: C679.2, U109.8
- new net N$364: D28.DO, LED_DO27.1
- new net N$365: Q29.5, R311.2
- new net N$366: Q29.2, R312.2
- new net N$367: C701.2, U113.45, X57.P1
- new net N$368: C702.2, U113.44, X57.P3
- new net N$369: C716.2, R310.1, U113.47
- new net N$370: R314.1, R315.2, U115.8
- new net N$371: R316.1, U115.9
- new net N$372: A29.FEED, C719.1, L29.1
- new net N$373: C720.1, L29.2, U113.2
- new net N$374: J29.A5, R317.2
- new net N$375: J29.B5, R318.2
- new net N$376: C704.2, U113.8
- new net N$377: D29.DO, LED_DO28.1
- new net N$378: Q30.5, R322.2
- new net N$379: Q30.2, R323.2
- new net N$380: C726.2, U117.45, X59.P1
- new net N$381: C727.2, U117.44, X59.P3
- new net N$382: C741.2, R321.1, U117.47
- new net N$383: R325.1, R326.2, U119.8
- new net N$384: R327.1, U119.9
- new net N$385: A30.FEED, C744.1, L30.1
- new net N$386: C745.1, L30.2, U117.2
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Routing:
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- added copper zone on layer 1, net GND20
- added copper zone on layer 15, net GND20
- added copper zone on layer 16, net GND20
- added copper zone on layer 2, net GND20
- added copper zone on layer 1, net GND21
- added copper zone on layer 15, net GND21
- added copper zone on layer 16, net GND21
- added copper zone on layer 2, net GND21
- added copper zone on layer 1, net GND22
- added copper zone on layer 15, net GND22
- added copper zone on layer 16, net GND22
- added copper zone on layer 2, net GND22
- added copper zone on layer 1, net GND23
- added copper zone on layer 15, net GND23
- added copper zone on layer 16, net GND23
- added copper zone on layer 2, net GND23
- added copper zone on layer 1, net GND24
- added copper zone on layer 15, net GND24
- added copper zone on layer 16, net GND24
- added copper zone on layer 2, net GND24
- added copper zone on layer 1, net GND25
- added copper zone on layer 15, net GND25
- added copper zone on layer 16, net GND25
- added copper zone on layer 2, net GND25
- added copper zone on layer 1, net GND26
- added copper zone on layer 15, net GND26
- added copper zone on layer 16, net GND26
- added copper zone on layer 2, net GND26
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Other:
- board size 187.2 x 95.5 mm -> 198.4 x 96 mm
- board text removed: "Route Out"

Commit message: Updates for JLCPCB manufacture
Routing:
- net CS39: track 43.0 -> 45.3 mm
- net CS93: track 43.0 -> 45.3 mm
- net CS9: track 43.0 -> 45.3 mm
- net CS6: track 43.0 -> 45.3 mm
- net CS42: track 43.0 -> 45.3 mm
- net CS36: track 43.0 -> 45.3 mm
- net CS27: track 43.0 -> 45.3 mm
- net CS24: track 43.0 -> 45.3 mm
- net CS84: track 43.0 -> 45.3 mm
- net CS78: track 43.0 -> 45.3 mm
- net CS48: track 43.0 -> 45.3 mm
- net CS30: track 43.0 -> 45.3 mm
- net CS3: track 43.0 -> 45.3 mm
- net CS0: track 43.0 -> 45.3 mm
- net CS90: track 43.0 -> 45.3 mm
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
